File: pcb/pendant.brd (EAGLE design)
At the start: 38.1 x 30.1 mm, 10 parts, among them IC1 TINY22S

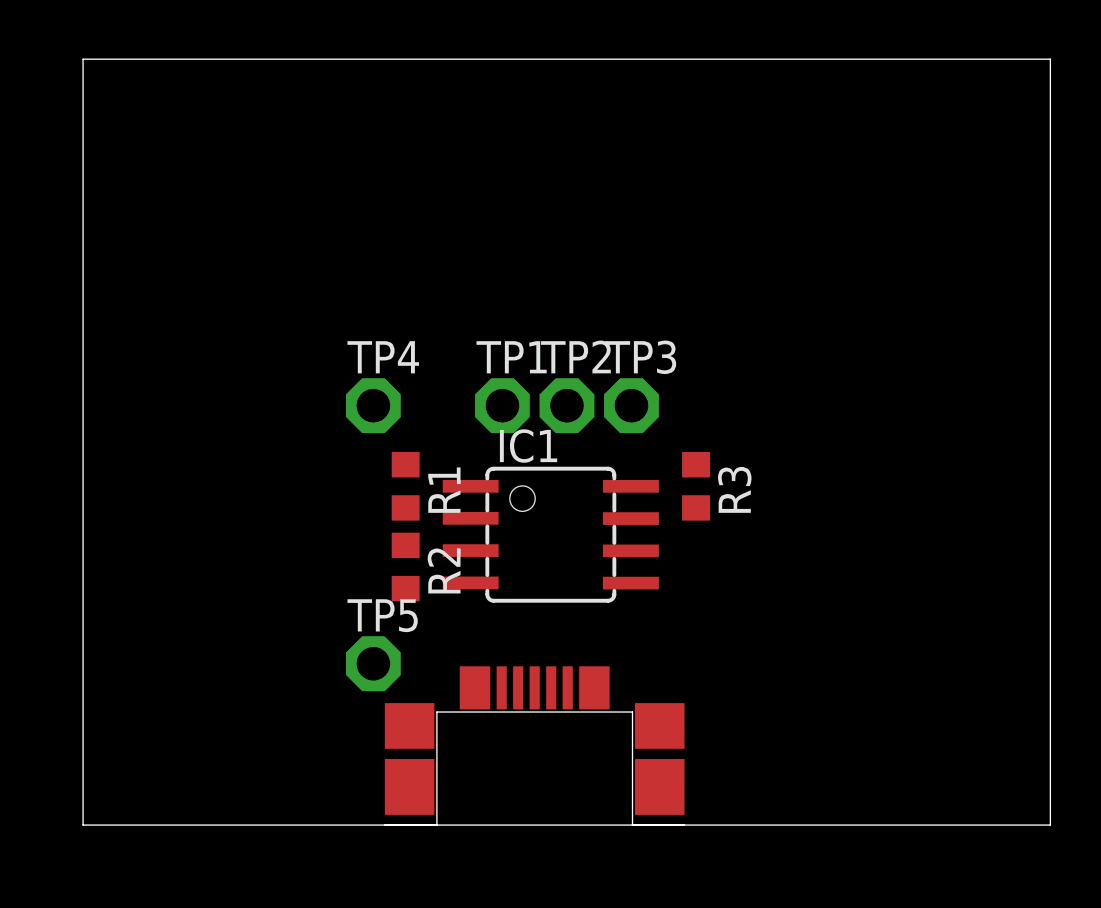
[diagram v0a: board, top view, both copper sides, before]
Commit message: added square cutout magnet, worked on board outline
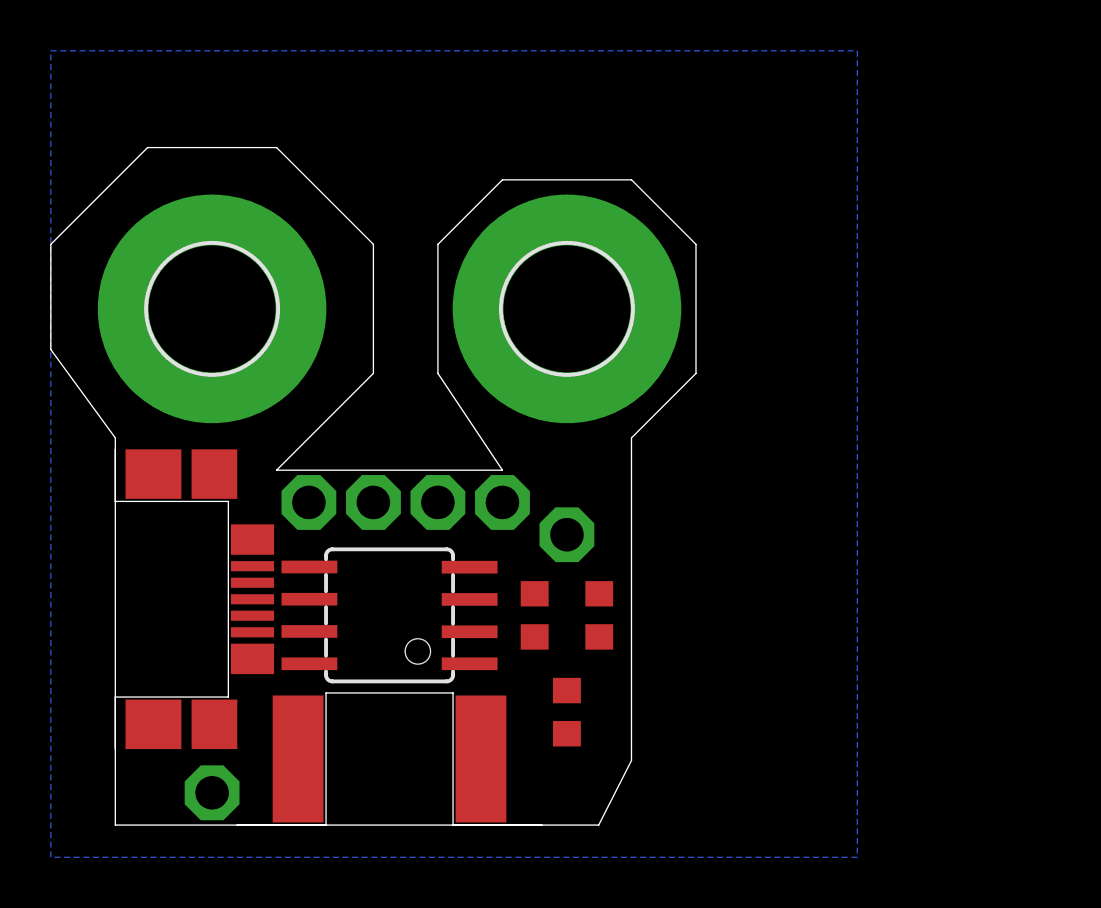
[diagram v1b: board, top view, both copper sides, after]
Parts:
- removed TP1, TP2, TP3: TPPAD1-13, testpad:P1-13
- added BLUE, GREEN, RED, TP6: TPPAD1-13, testpad:P1-13
- added H1, H2: MOUNT-PAD-ROUND5.0, holes:5,0-PAD
- added U$2: MAGNET, pendant:5MM-SQUARE
- moved U$1 18.8 mm to (1.27, 8.89), turned to 270 degrees
- moved TP4 9.16 mm to (19.1, 11.4)
- moved R2 8.54 mm to (19.1, 4.45)
- moved TP5 8.13 mm to (5.08, 1.27)
- moved R1 7.18 mm to (17.8, 8.26)
- moved IC1 7.10 mm to (12.1, 8.26), turned to 90 degrees
- moved R3 6.35 mm to (20.3, 8.26)
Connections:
- net +3V3: now also U$2.P1, U$2.P2
- net BLUE: now also BLUE.TP; no longer TP3.TP
- net GND: now also H1.B5, H2.B5, TP6.TP
- net GREEN: now also GREEN.TP; no longer TP2.TP
- net RED: now also RED.TP; no longer TP1.TP
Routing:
- added copper zone on layer 16, net GND
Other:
- board size 38.1 x 30.1 mm -> 25.4 x 26.7 mm

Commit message: switch to 8th-inch magnet
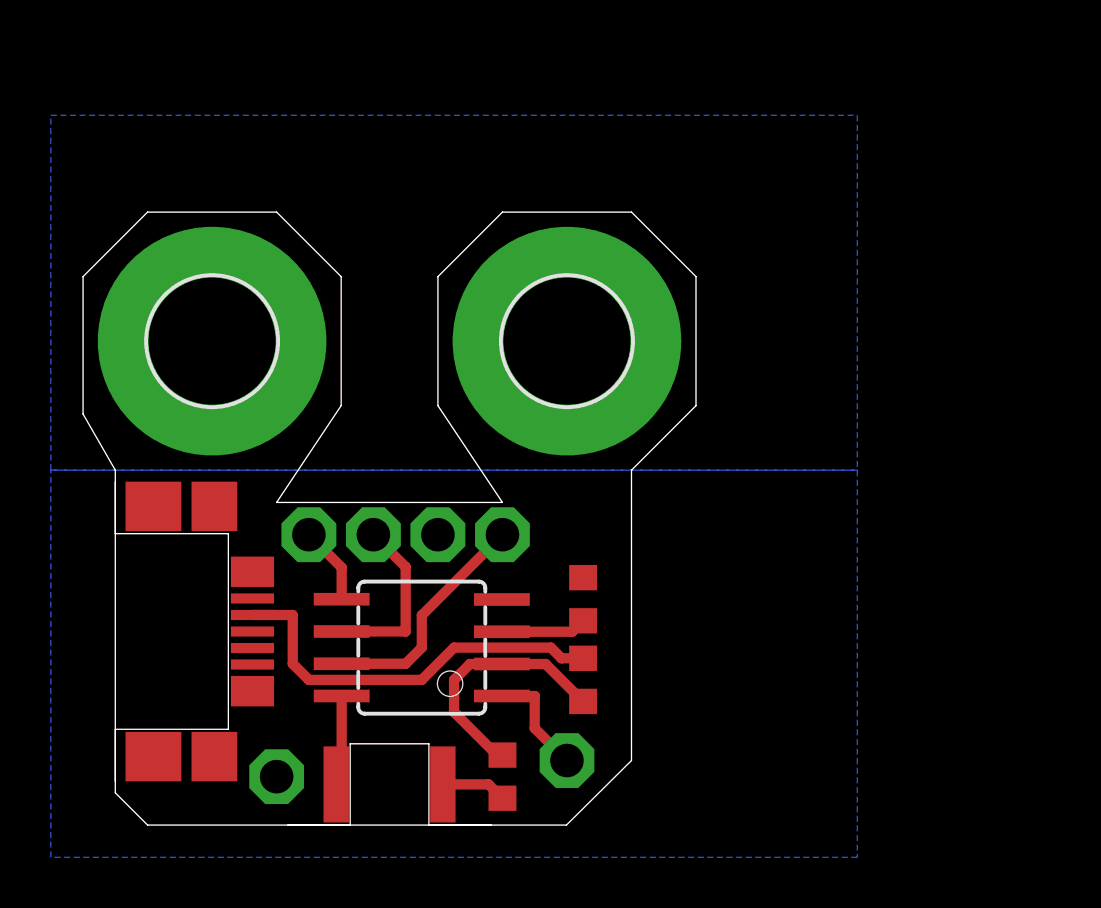
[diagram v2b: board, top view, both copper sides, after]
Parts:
- U$2: value MAGNET -> MAGNET8TH-INCH; device pendant:5MM-SQUARE -> pendant:8TH-SQUARE
- moved TP4 8.89 mm to (19.1, 2.54)
- moved BLUE 7.73 mm to (8.89, 11.4)
- moved RED 7.73 mm to (16.5, 11.4)
- moved R3 7.41 mm to (16.5, 1.91)
- moved R2 4.49 mm to (19.7, 8.89), turned to 90 degrees
- moved R1 3.17 mm to (19.7, 5.71), turned to 90 degrees
- moved TP5 2.62 mm to (7.62, 1.91)
- moved IC1 1.80 mm to (13.3, 6.99)
- moved U$1 1.27 mm to (1.27, 7.62)
- moved GREEN 1.27 mm to (11.4, 11.4)
- moved H1 1.27 mm to (5.08, 19.1)
- moved H2 1.27 mm to (19.1, 19.1)
- moved TP6 1.27 mm to (14.0, 11.4)
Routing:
- net N$1: track 0.00 -> 15.9 mm
- net N$3: track 0.00 -> 9.82 mm
- net RED: track 0.00 -> 9.18 mm
- net GREEN: track 0.00 -> 6.86 mm
- net +3V3: track 0.00 -> 6.14 mm
- net N$5: track 0.00 -> 4.36 mm
- net N$4: track 0.00 -> 3.37 mm
- net BLUE: track 0.00 -> 3.07 mm
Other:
- board size 25.4 x 26.7 mm -> 24.1 x 24.1 mm

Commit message: fix usb wiring bug; fully routed
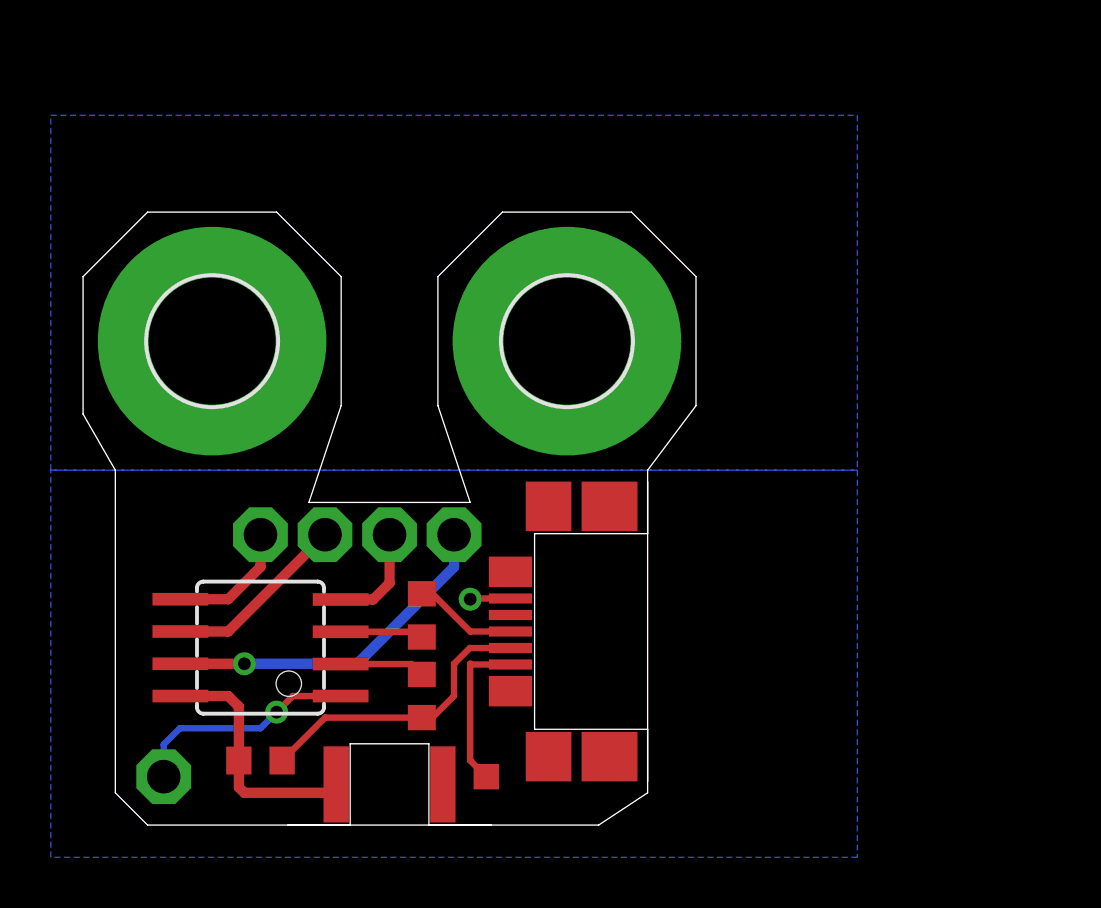
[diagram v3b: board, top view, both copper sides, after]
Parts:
- TP5: value TPPAD1-13 -> TPTP10SQ; device testpad:P1-13 -> testpad:TP10SQ
- moved U$1 21.0 mm to (22.2, 7.62), turned to 90 degrees
- moved TP4 15.9 mm to (3.17, 1.91)
- moved R3 9.55 mm to (6.99, 2.54), turned to 180 degrees
- moved TP5 8.25 mm to (15.9, 1.91)
- moved R1 6.38 mm to (13.3, 5.08), turned to 270 degrees
- moved R2 6.38 mm to (13.3, 8.26)
- moved IC1 6.35 mm to (6.99, 6.99)
- moved RED 1.91 mm to (14.6, 11.4)
- moved TP6 1.91 mm to (12.1, 11.4)
- moved BLUE 1.91 mm to (6.99, 11.4)
- moved GREEN 1.90 mm to (9.53, 11.4)
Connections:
- net N$1: now also R3.1
- net N$3: no longer R3.1
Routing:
- net N$3: track 9.82 -> 3.37 mm
- net N$6: track 0.00 -> 6.31 mm
- net GND: track 0.00 -> 5.70 mm, vias 0 -> 1
- net N$5: track 4.36 -> 9.02 mm, vias 0 -> 1
- net RED: track 9.18 -> 13.6 mm, vias 0 -> 1
- net N$1: track 15.9 -> 11.6 mm
- net N$2: track 0.00 -> 4.11 mm
- net +3V3: track 6.14 -> 9.71 mm
- net BLUE: track 3.07 -> 4.95 mm
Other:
- outline, holes or cut-outs redrawn
